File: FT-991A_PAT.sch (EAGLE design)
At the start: 34 parts, among them Q1 J310, Q2 BFS17, U2 SN74AHC1G08_DCK_5, X1 SCP_OUT, X2 IF_IN

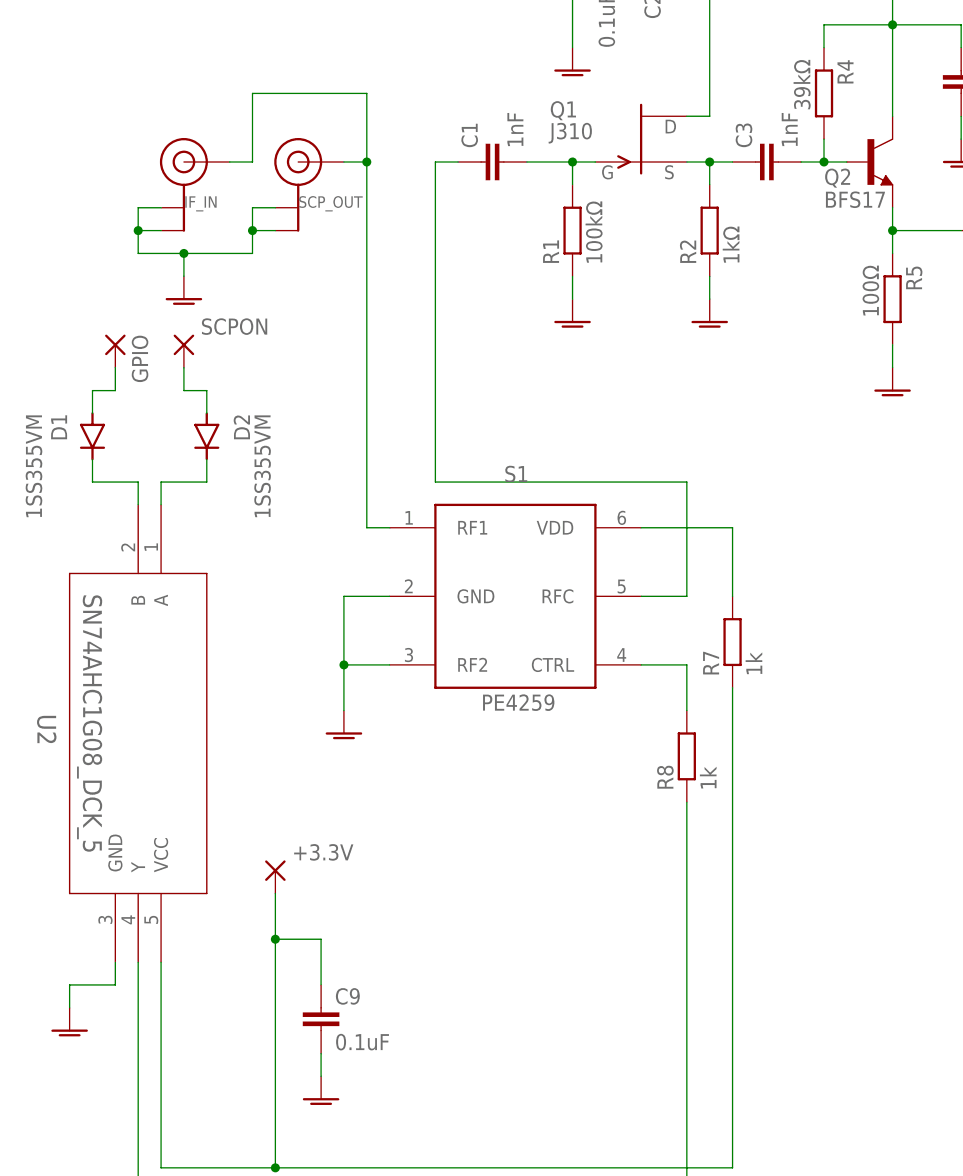
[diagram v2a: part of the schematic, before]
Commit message: Revision F
* Added 1 nF capacitors in RF lines in PE4529 (except RF2, goes with a
  470 pF to GND)
* Got rid of the VCC via which was crossing the RF line (argh)
* Finally got the courage to change a bit the board layout and escape
  from the thin strip that I was working previously.
* And another THANK YOU to Gordon AD5GG for his invaluable feedback and
  help.
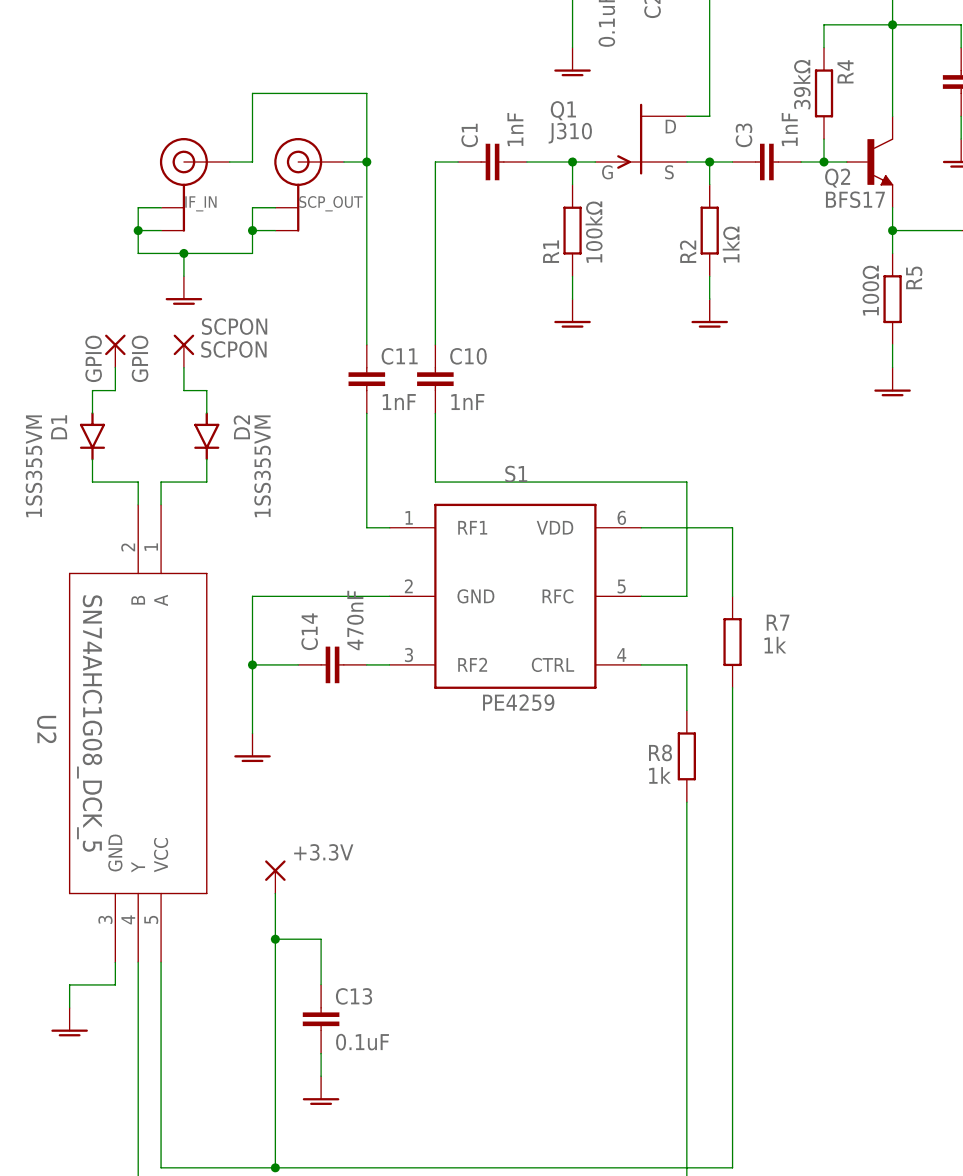
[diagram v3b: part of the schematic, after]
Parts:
- added C10, C11: 1nF, rcl:C-EUC0805K
- added C14: 470nF, rcl:C-EUC0805K
- GPIO: value WIREPADSMD1,27-254 -> GPIO
- SCPON: value WIREPADSMD1,27-254 -> SCPON
- renumbered C9 to C13
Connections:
- new net N$14: C1.1, C10.1
- new net N$21: C11.2, S1.RF1
- new net N$24: C14.2, S1.RF2
- net GNDA: now also C14.1; no longer S1.RF2
- net N$15: now also C10.2; no longer C1.1
- net N$7: now also C11.1; no longer S1.RF1
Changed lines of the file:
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@@
 <attribute name="PROJECT_INFO" value="Yaesu FT-991A Panadapter with Signal Control"/>
 <attribute name="PROJECT_NAME" value="FT-991A PAT &amp; SDR"/>
-<attribute name="REVISION_ID" value="E"/>
+<attribute name="REVISION_ID" value="F"/>
 </attributes>
 <variantdefs>
@@
 <part name="D2" library="diode" library_urn="urn:adsk.eagle:library:210" deviceset="DIODE-" device="SOD323-W" package3d_urn="urn:adsk.eagle:package:43418/1" value="1SS355VM"/>
 <part name="GND13" library="supply1" library_urn="urn:adsk.eagle:library:371" deviceset="GNDA" device=""/>
-<part name="C9" library="rcl" library_urn="urn:adsk.eagle:library:334" deviceset="C-EU" device="C0805K" package3d_urn="urn:adsk.eagle:package:23681/2" value="0.1uF"/>
 <part name="GND10" library="supply1" library_urn="urn:adsk.eagle:library:371" deviceset="GNDA" device=""/>
 <part name="GND12" library="supply1" library_urn="urn:adsk.eagle:library:371" deviceset="GNDA" device=""/>
-<part name="GPIO" library="wirepad" library_urn="urn:adsk.eagle:library:412" deviceset="WIREPAD" device="SMD1,27-254" package3d_urn="urn:adsk.eagle:package:30839/1" value=""/>
-<part name="SCPON" library="wirepad" library_urn="urn:adsk.eagle:library:412" deviceset="WIREPAD" device="SMD1,27-254" package3d_urn="urn:adsk.eagle:package:30839/1" value=""/>
+<part name="GPIO" library="wirepad" library_urn="urn:adsk.eagle:library:412" deviceset="WIREPAD" device="SMD1,27-254" package3d_urn="urn:adsk.eagle:package:30839/1" value="GPIO"/>
+<part name="SCPON" library="wirepad" library_urn="urn:adsk.eagle:library:412" deviceset="WIREPAD" device="SMD1,27-254" package3d_urn="urn:adsk.eagle:package:30839/1" value="SCPON"/>
 <part name="+3.3V" library="wirepad" library_urn="urn:adsk.eagle:library:412" deviceset="WIREPAD" device="SMD1,27-254" package3d_urn="urn:adsk.eagle:package:30839/1" value=""/>
 <part name="S1" library="psemi" deviceset="PE4259" device="" value="PE4259"/>
 <part name="R7" library="rcl" deviceset="R-EU_" device="R0805" value="1k"/>
 <part name="R8" library="rcl" deviceset="R-EU_" device="R0805" value="1k"/>
+<part name="C13" library="rcl" deviceset="C-EU" device="C0805K" value="0.1uF"/>
+<part name="C14" library="rcl" deviceset="C-EU" device="C0805K" value="470nF"/>
+<part name="C10" library="rcl" deviceset="C-EU" device="C0805K" value="1nF"/>
+<part name="C11" library="rcl" deviceset="C-EU" device="C0805K" value="1nF"/>
 </parts>
 <sheets>
@@
 </instance>
 <instance part="GND13" gate="1" x="93.98" y="25.4" smashed="yes"/>
-<instance part="C9" gate="G$1" x="93.98" y="35.56" smashed="yes">
-<attribute name="NAME" x="95.504" y="35.941" size="1.778" layer="95"/>
-<attribute name="VALUE" x="95.504" y="30.861" size="1.778" layer="96"/>
-</instance>
 <instance part="GND10" gate="1" x="66.04" y="33.02" smashed="yes"/>
-<instance part="GND12" gate="1" x="96.52" y="66.04" smashed="yes"/>
+<instance part="GND12" gate="1" x="86.36" y="63.5" smashed="yes"/>
 <instance part="GPIO" gate="G$1" x="71.12" y="109.22" smashed="yes" rot="R270">
 <attribute name="NAME" x="72.9742" y="110.363" size="1.778" layer="95" rot="R270"/>
@@
 </instance>
 <instance part="R7" gate="G$1" x="139.7" y="76.2" smashed="yes" rot="R90">
-<attribute name="NAME" x="138.2014" y="72.39" size="1.778" layer="95" rot="R90"/>
-<attribute name="VALUE" x="143.002" y="72.39" size="1.778" layer="96" rot="R90"/>
+<attribute name="NAME" x="143.2814" y="77.47" size="1.778" layer="95"/>
+<attribute name="VALUE" x="143.002" y="74.93" size="1.778" layer="96"/>
 </instance>
 <instance part="R8" gate="G$1" x="134.62" y="63.5" smashed="yes" rot="R90">
-<attribute name="NAME" x="133.1214" y="59.69" size="1.778" layer="95" rot="R90"/>
-<attribute name="VALUE" x="137.922" y="59.69" size="1.778" layer="96" rot="R90"/>
+<attribute name="NAME" x="133.1214" y="64.77" size="1.778" layer="95" rot="R180"/>
+<attribute name="VALUE" x="132.842" y="62.23" size="1.778" layer="96" rot="R180"/>
+</instance>
+<instance part="C13" gate="G$1" x="93.98" y="35.56" smashed="yes">
+<attribute name="NAME" x="95.504" y="35.941" size="1.778" layer="95"/>
+<attribute name="VALUE" x="95.504" y="30.861" size="1.778" layer="96"/>
+</instance>
+<instance part="C14" gate="G$1" x="93.98" y="73.66" smashed="yes" rot="R90">
+<attribute name="NAME" x="93.599" y="75.184" size="1.778" layer="95" rot="R90"/>
+<attribute name="VALUE" x="98.679" y="75.184" size="1.778" layer="96" rot="R90"/>
+</instance>
+<instance part="C10" gate="G$1" x="106.68" y="106.68" smashed="yes">
+<attribute name="NAME" x="108.204" y="107.061" size="1.778" layer="95"/>
+<attribute name="VALUE" x="108.204" y="101.981" size="1.778" layer="96"/>
+</instance>
+<instance part="C11" gate="G$1" x="99.06" y="106.68" smashed="yes">
+<attribute name="NAME" x="100.584" y="107.061" size="1.778" layer="95"/>
+<attribute name="VALUE" x="100.584" y="101.981" size="1.778" layer="96"/>
 </instance>
 </instances>
@@
 </segment>
 <segment>
-<pinref part="C9" gate="G$1" pin="2"/>
 <pinref part="GND13" gate="1" pin="GNDA"/>
 <wire x1="93.98" y1="30.48" x2="93.98" y2="27.94" width="0.1524" layer="91"/>
+<pinref part="C13" gate="G$1" pin="2"/>
 </segment>
 <segment>
@@
 <pinref part="S1" gate="G$1" pin="GND"/>
 <pinref part="GND12" gate="1" pin="GNDA"/>
-<wire x1="101.6" y1="81.28" x2="96.52" y2="81.28" width="0.1524" layer="91"/>
-<wire x1="96.52" y1="81.28" x2="96.52" y2="73.66" width="0.1524" layer="91"/>
-<pinref part="S1" gate="G$1" pin="RF2"/>
-<wire x1="96.52" y1="73.66" x2="96.52" y2="68.58" width="0.1524" layer="91"/>
-<wire x1="101.6" y1="73.66" x2="96.52" y2="73.66" width="0.1524" layer="91"/>
-<junction x="96.52" y="73.66"/>
+<wire x1="101.6" y1="81.28" x2="86.36" y2="81.28" width="0.1524" layer="91"/>
+<wire x1="86.36" y1="81.28" x2="86.36" y2="73.66" width="0.1524" layer="91"/>
+<wire x1="86.36" y1="73.66" x2="86.36" y2="66.04" width="0.1524" layer="91"/>
+<wire x1="91.44" y1="73.66" x2="86.36" y2="73.66" width="0.1524" layer="91"/>
+<junction x="86.36" y="73.66"/>
+<pinref part="C14" gate="G$1" pin="1"/>
 </segment>
 </net>
@@
 <wire x1="88.9" y1="48.26" x2="88.9" y2="43.18" width="0.1524" layer="91"/>
 <wire x1="88.9" y1="43.18" x2="93.98" y2="43.18" width="0.1524" layer="91"/>
-<pinref part="C9" gate="G$1" pin="1"/>
 <wire x1="93.98" y1="43.18" x2="93.98" y2="38.1" width="0.1524" layer="91"/>
 <pinref part="+3.3V" gate="G$1" pin="P"/>
@@
 <wire x1="139.7" y1="17.78" x2="139.7" y2="71.12" width="0.1524" layer="91"/>
 <pinref part="R7" gate="G$1" pin="1"/>
+<pinref part="C13" gate="G$1" pin="1"/>
 </segment>
 </net>
@@
 <pinref part="X2" gate="G$1" pin="SIGNAL"/>
 <wire x1="83.82" y1="129.54" x2="86.36" y2="129.54" width="0.1524" layer="91"/>
-<pinref part="S1" gate="G$1" pin="RF1"/>
 <wire x1="99.06" y1="137.16" x2="99.06" y2="129.54" width="0.1524" layer="91"/>
-<wire x1="99.06" y1="129.54" x2="99.06" y2="88.9" width="0.1524" layer="91"/>
-<wire x1="99.06" y1="88.9" x2="101.6" y2="88.9" width="0.1524" layer="91"/>
 <pinref part="X1" gate="G$1" pin="SIGNAL"/>
 <wire x1="96.52" y1="129.54" x2="99.06" y2="129.54" width="0.1524" layer="91"/>
 <junction x="99.06" y="129.54"/>
+<wire x1="99.06" y1="129.54" x2="99.06" y2="109.22" width="0.1524" layer="91"/>
+<pinref part="C11" gate="G$1" pin="1"/>
 </segment>
 </net>
 <net name="N$15" class="0">
 <segment>
-<pinref part="C1" gate="G$1" pin="1"/>
-<wire x1="106.68" y1="129.54" x2="109.22" y2="129.54" width="0.1524" layer="91"/>
-<wire x1="106.68" y1="129.54" x2="106.68" y2="93.98" width="0.1524" layer="91"/>
 <wire x1="106.68" y1="93.98" x2="134.62" y2="93.98" width="0.1524" layer="91"/>
 <pinref part="S1" gate="G$1" pin="RFC"/>
 <wire x1="134.62" y1="93.98" x2="134.62" y2="81.28" width="0.1524" layer="91"/>
 <wire x1="134.62" y1="81.28" x2="129.54" y2="81.28" width="0.1524" layer="91"/>
+<wire x1="106.68" y1="101.6" x2="106.68" y2="93.98" width="0.1524" layer="91"/>
+<pinref part="C10" gate="G$1" pin="2"/>
 </segment>
 </net>
@@
 </segment>
 </net>
+<net name="N$14" class="0">
+<segment>
+<pinref part="C1" gate="G$1" pin="1"/>
+<wire x1="106.68" y1="129.54" x2="109.22" y2="129.54" width="0.1524" layer="91"/>
+<wire x1="106.68" y1="129.54" x2="106.68" y2="109.22" width="0.1524" layer="91"/>
+<pinref part="C10" gate="G$1" pin="1"/>
+</segment>
+</net>
+<net name="N$21" class="0">
+<segment>
+<pinref part="S1" gate="G$1" pin="RF1"/>
+<wire x1="99.06" y1="88.9" x2="101.6" y2="88.9" width="0.1524" layer="91"/>
+<wire x1="99.06" y1="101.6" x2="99.06" y2="88.9" width="0.1524" layer="91"/>
+<pinref part="C11" gate="G$1" pin="2"/>
+</segment>
+</net>
+<net name="N$24" class="0">
+<segment>
+<pinref part="S1" gate="G$1" pin="RF2"/>
+<wire x1="101.6" y1="73.66" x2="99.06" y2="73.66" width="0.1524" layer="91"/>
+<pinref part="C14" gate="G$1" pin="2"/>
+</segment>
+</net>

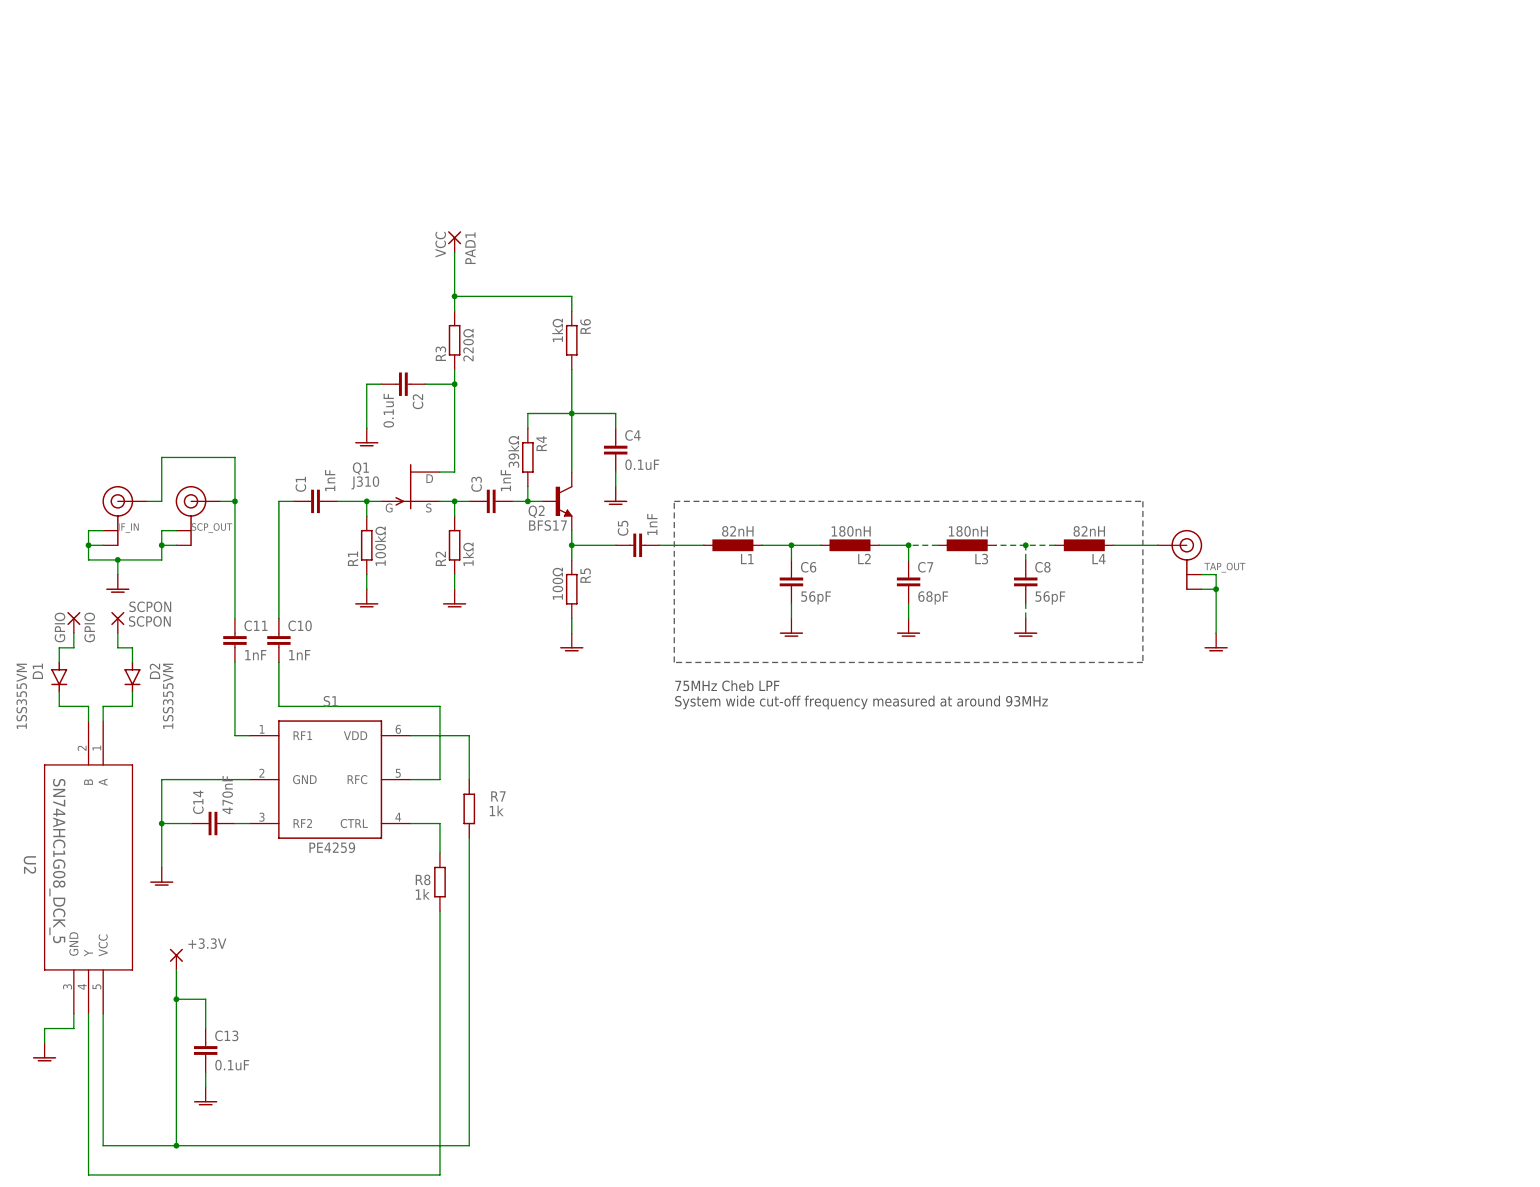
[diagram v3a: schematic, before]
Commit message: New files, correction, better schematic layout
Still in Revision F:
* Fixed C14 values (it is 4.7 nF and not 470 pF)
* Cleaner and unified board layout
* Identified properly Q1 (it is a J310)
* A few tweaks and spam in board silk screen
* Added project's PDF and board's PNG images
... And that's all, folks! \o
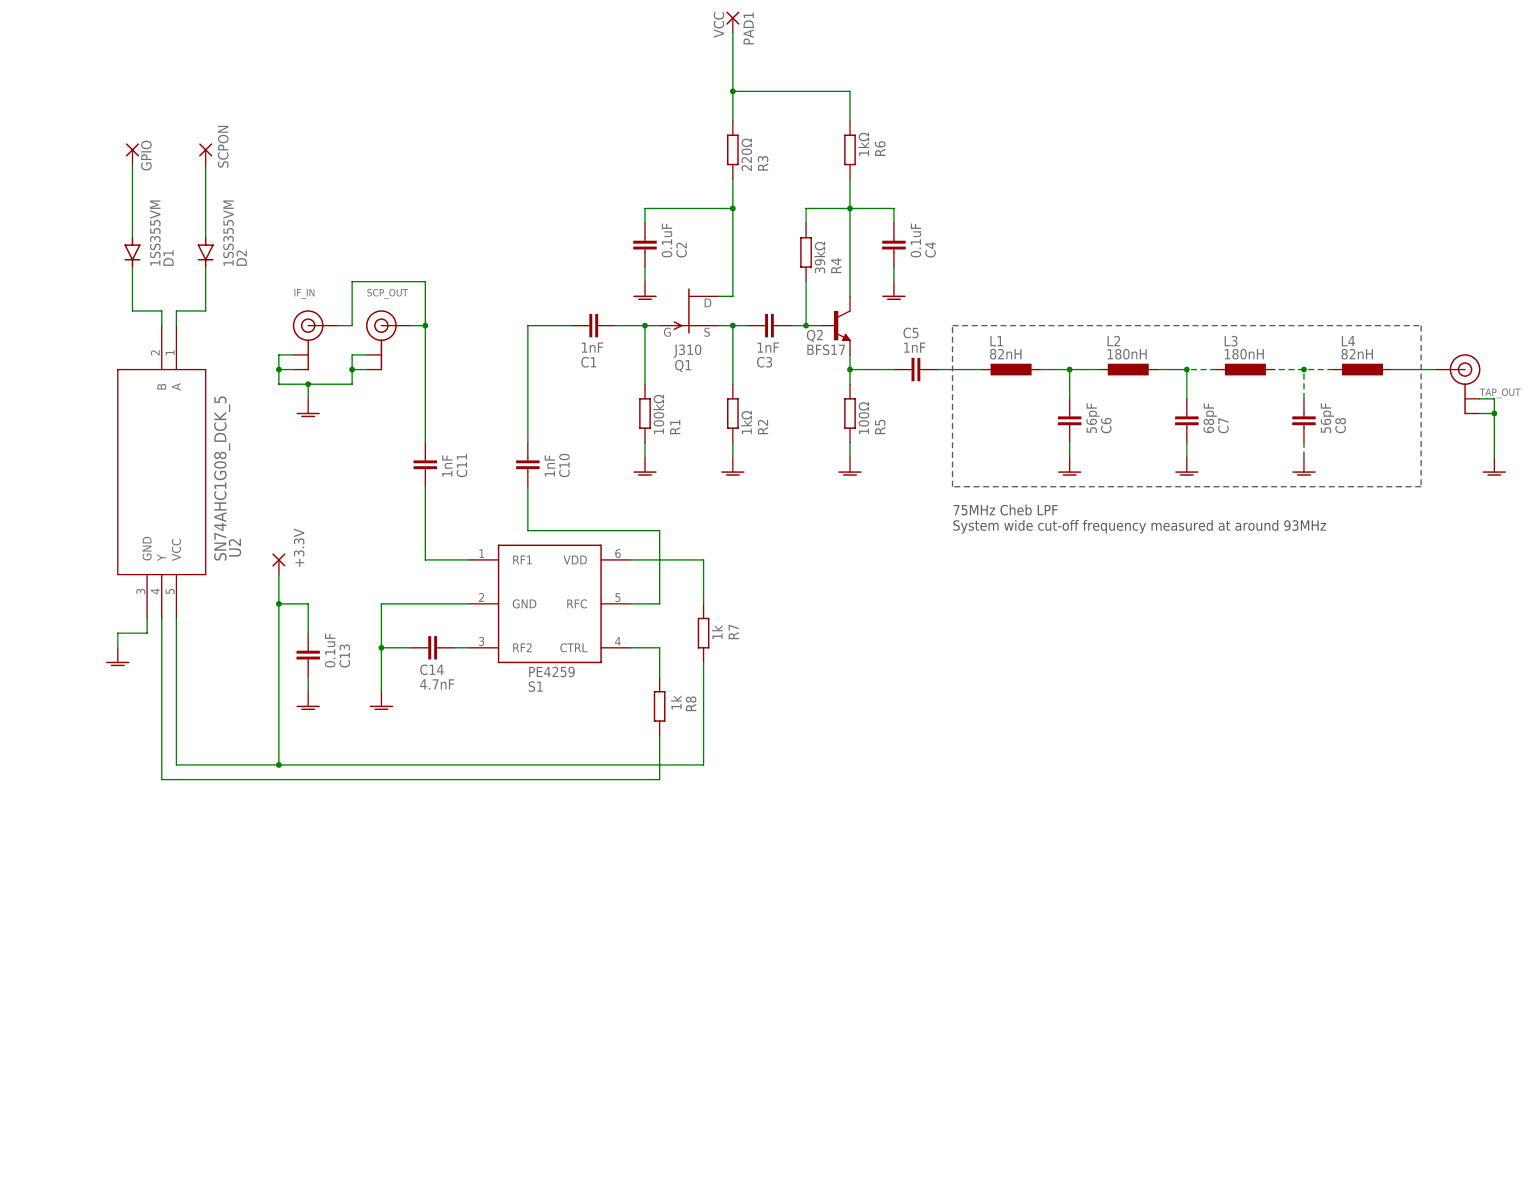
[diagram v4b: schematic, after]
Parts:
- C14: value 470nF -> 4.7nF
- Q1: SPICEPREFIX (none) -> J
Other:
- moved on the sheet: +3.3V, C1, C10, C11, C13, C14, C2, C3, C4, C5, C6, C7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
